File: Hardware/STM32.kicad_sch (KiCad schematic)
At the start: 70 parts, among them IC1 STTS22HTR, SW1 SW_Push_Dual, U3 STM32L4R5ZITx, Y2 TG-3541CE_32.7680KXB3, Y3 ECS-TXO-2520-33-250-AN-TR

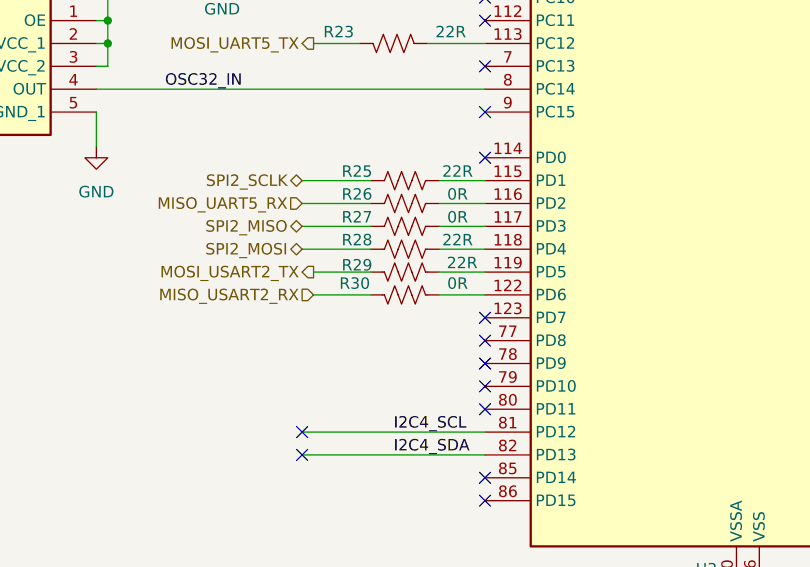
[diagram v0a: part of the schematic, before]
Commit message: Replace Optical Downlink with ADCS Sensors connector
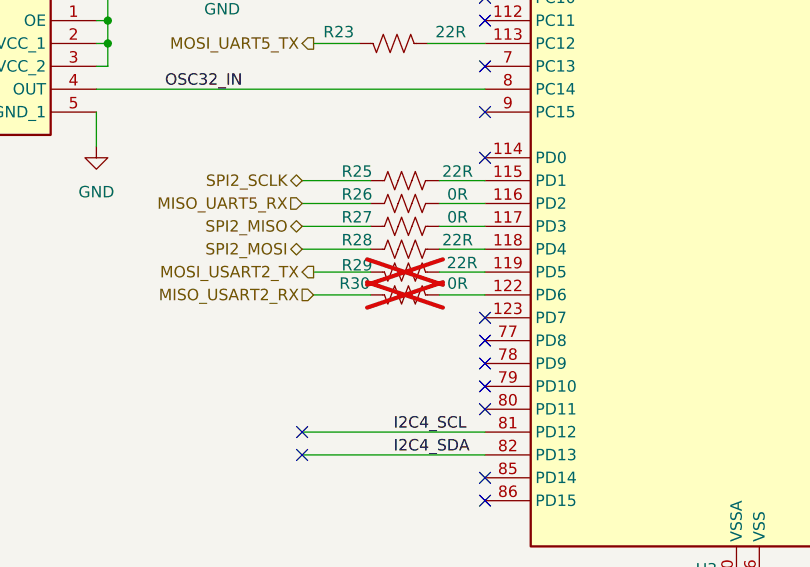
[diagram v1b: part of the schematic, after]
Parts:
- R29, R30: now not fitted
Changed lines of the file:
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@@
 		(in_bom yes)
 		(on_board yes)
-		(dnp no)
+		(dnp yes)
 		(property "Reference" "R29"
 			(at 172.466 215.138 90)
@@
 		(in_bom yes)
 		(on_board yes)
-		(dnp no)
+		(dnp yes)
 		(property "Reference" "R30"
 			(at 172.212 217.17 90)

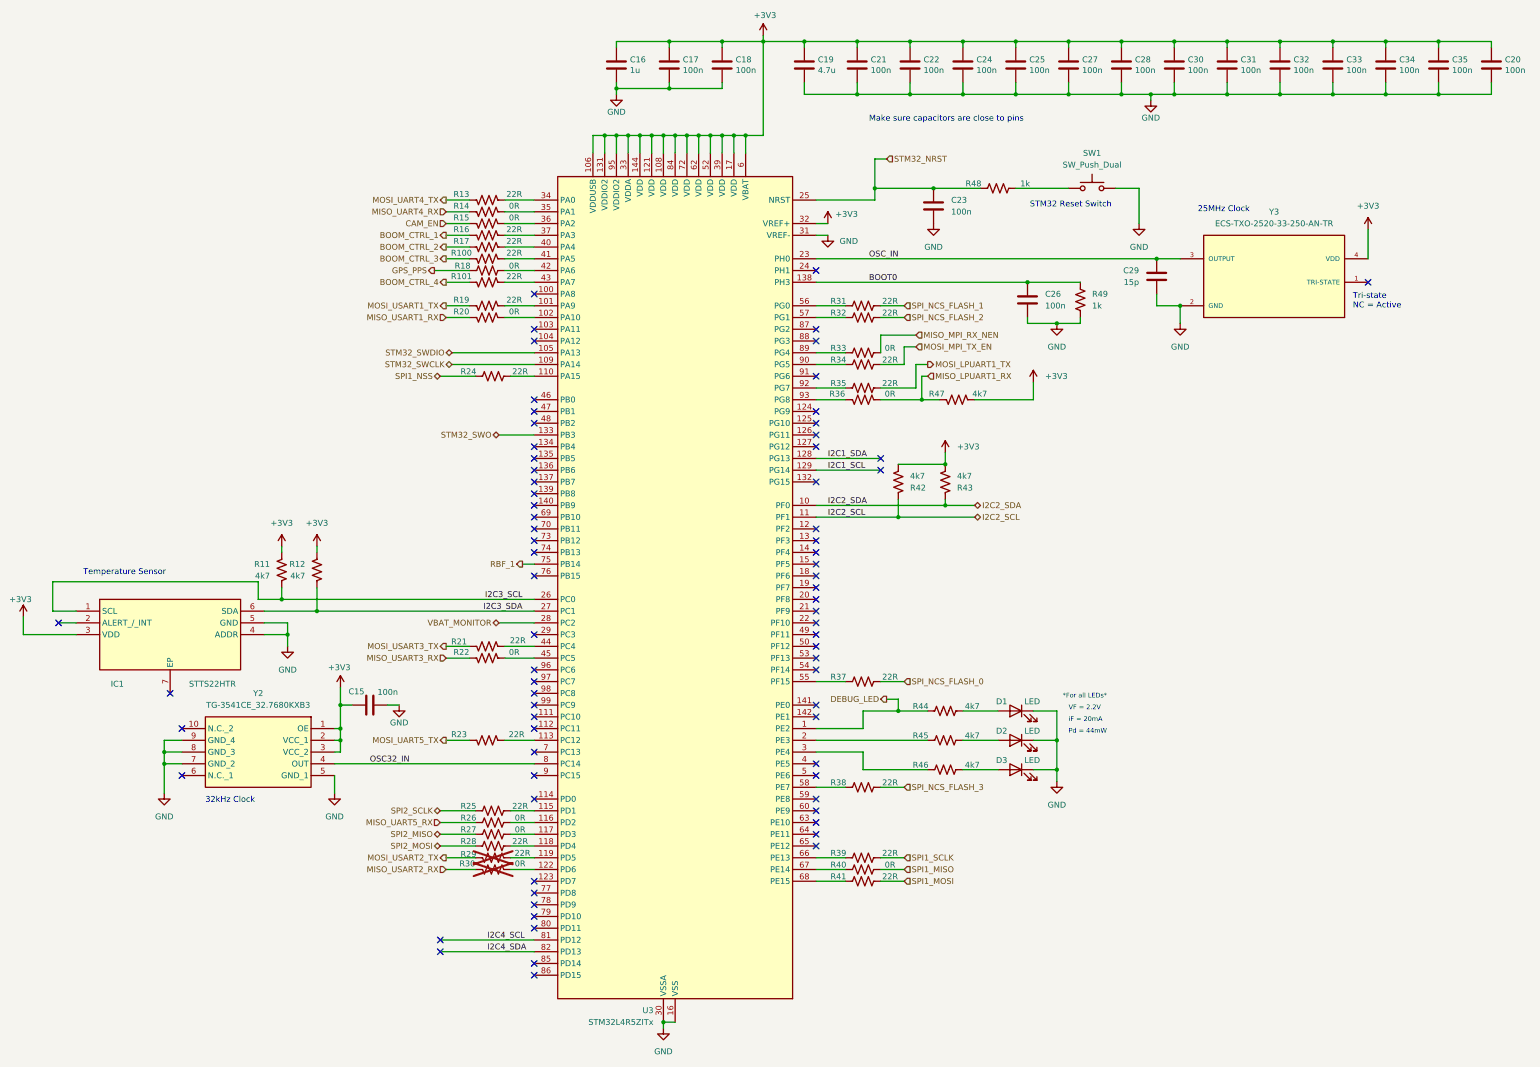
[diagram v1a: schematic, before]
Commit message: Update schematic to allow using STM32 alone
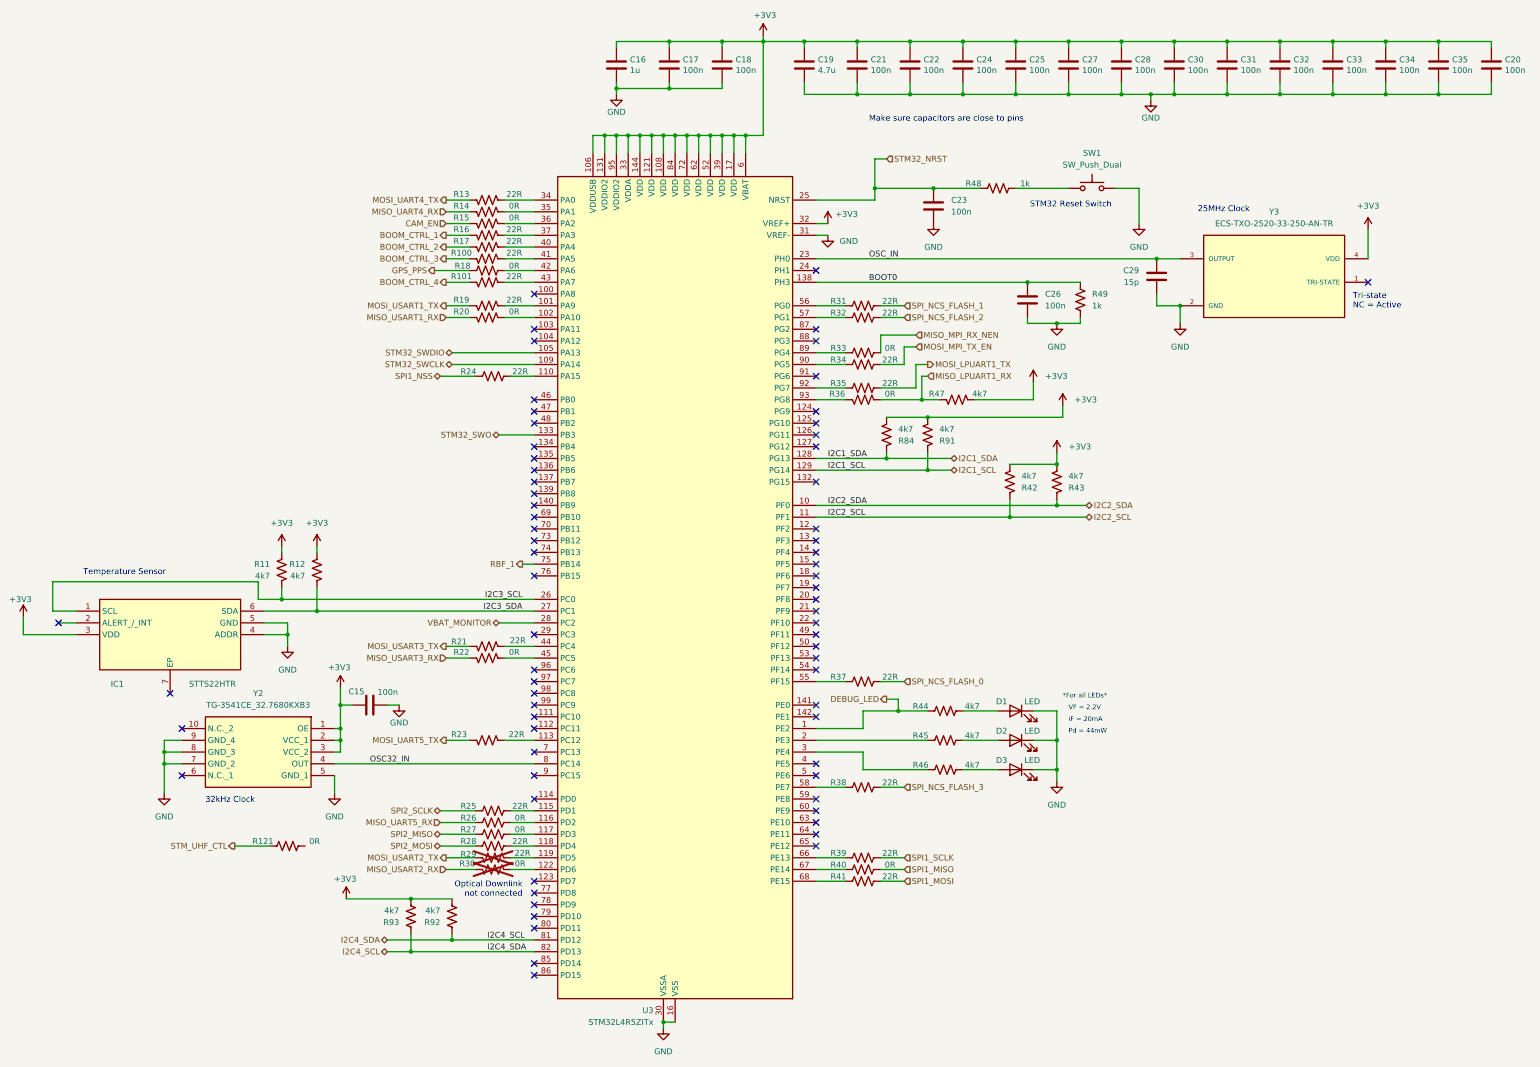
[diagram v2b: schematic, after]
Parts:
- added R121: 0R, Resistor_SMD:R_0603_1608Metric, symbol Device:R_US
- added R84, R91, R92, R93: 4k7, Resistor_SMD:R_0603_1608Metric, symbol Device:R_US
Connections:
- net I2C4_SDA is gone; now on net I2C4_SCL: U3.82 (PD13)
- net +3V3: now also R84.2, R91.2, R92.2, R93.2
- net I2C1_SCL: now also R91.1
- net I2C1_SDA: now also R84.1
- net I2C4_SCL: now also R92.1, R93.1
- new net STM_UHF_CTL: R121.1
- no-connect marks 74 -> 70
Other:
- note added: "Optical Downlink not connected"
- moved on the sheet: R42, R43

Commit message: Populate more resistors
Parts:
- removed R121: 0R, Resistor_SMD:R_0603_1608Metric, symbol Device:R_US
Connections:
- net I2C4_SCL: no longer R93.1, U3.82 (PD13)
- new net I2C4_SDA: R93.1, U3.82 (PD13)
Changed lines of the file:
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@@
 		)
 	)
-	(hierarchical_label "I2C4_SDA"
+	(hierarchical_label "I2C4_SCL"
 		(shape bidirectional)
 		(at 154.94 233.68 180)
@@
 		)
 	)
-	(hierarchical_label "I2C4_SCL"
+	(hierarchical_label "I2C4_SDA"
 		(shape bidirectional)
 		(at 154.94 236.22 180)
@@
 					(unit 1)
 				)
-			)
-		)
-	)
-	(symbol
-		(lib_id "Device:R_US")
-		(at 133.35 213.36 90)
-		(unit 1)
-		(exclude_from_sim no)
-		(in_bom yes)
-		(on_board yes)
-		(dnp no)
-		(property "Reference" "R121"
-			(at 128.016 212.344 90)
-			(effects
-				(font
-					(size 1.27 1.27)
-				)
-			)
-		)
-		(property "Value" "0R"
-			(at 139.192 212.344 90)
-			(effects
-				(font
-					(size 1.27 1.27)
-				)
-			)
-		)
-		(property "Footprint" "Resistor_SMD:R_0603_1608Metric"
-			(at 133.604 212.344 90)
-			(effects
-				(font
-					(size 1.27 1.27)
-				)
-				(hide yes)
-			)
-		)
-		(property "Datasheet" "~"
-			(at 133.35 213.36 0)
-			(effects
-				(font
-					(size 1.27 1.27)
-				)
-				(hide yes)
-			)
-		)
-		(property "Description" "Resistor, US symbol"
-			(at 133.35 213.36 0)
-			(effects
-				(font
-					(size 1.27 1.27)
-				)
-				(hide yes)
-			)
-		)
-		(pin "2"
-		)
-		(pin "1"
-		)
-		(instances
-			(project "CTS-SAT-2-OBC-PCB"
-				(path "/58243925-df8d-4fc1-899e-fce866d1d25a/c7b2a9f5-c39c-4892-aa33-31b3626fafef"
-					(reference "R121")
-					(unit 1)
-				)

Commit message: route most connectors
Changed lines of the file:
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@@
 	(wire
 		(pts
+			(xy 334.01 151.13) (xy 331.47 151.13)
+		)
+		(stroke
+			(width 0)
+			(type default)
+		)
+	)
+	(wire
+		(pts
 			(xy 290.83 50.8) (xy 279.4 50.8)
 		)
@@
 	(wire
 		(pts
+			(xy 334.01 148.59) (xy 331.47 148.59)
+		)
+		(stroke
+			(width 0)
+			(type default)
+		)
+	)
+	(wire
+		(pts
 			(xy 302.26 39.37) (xy 313.69 39.37)
 		)
@@
 	(wire
 		(pts
+			(xy 334.01 166.37) (xy 331.47 166.37)
+		)
+		(stroke
+			(width 0)
+			(type default)
+		)
+	)
+	(wire
+		(pts
 			(xy 232.41 59.69) (xy 232.41 63.5)
 		)
@@
 	(wire
 		(pts
+			(xy 334.01 161.29) (xy 331.47 161.29)
+		)
+		(stroke
+			(width 0)
+			(type default)
+		)
+	)
+	(wire
+		(pts
 			(xy 261.62 106.68) (xy 261.62 102.87)
 		)
@@
 	(wire
 		(pts
+			(xy 334.01 163.83) (xy 331.47 163.83)
+		)
+		(stroke
+			(width 0)
+			(type default)
+		)
+	)
+	(wire
+		(pts
 			(xy 180.34 88.9) (xy 186.69 88.9)
 		)
@@
 	(wire
 		(pts
+			(xy 334.01 158.75) (xy 331.47 158.75)
+		)
+		(stroke
+			(width 0)
+			(type default)
+		)
+	)
+	(wire
+		(pts
 			(xy 215.9 49.53) (xy 215.9 48.26)
 		)
@@
 	(wire
 		(pts
+			(xy 334.01 153.67) (xy 331.47 153.67)
+		)
+		(stroke
+			(width 0)
+			(type default)
+		)
+	)
+	(wire
+		(pts
 			(xy 201.93 59.69) (xy 201.93 63.5)
 		)
@@
 	(wire
 		(pts
+			(xy 334.01 156.21) (xy 331.47 156.21)
+		)
+		(stroke
+			(width 0)
+			(type default)
+		)
+	)
+	(wire
+		(pts
 			(xy 289.56 138.43) (xy 289.56 142.24)
 		)
@@
 		)
 	)
+	(wire
+		(pts
+			(xy 334.01 168.91) (xy 331.47 168.91)
+		)
+		(stroke
+			(width 0)
+			(type default)
+		)
+	)
 	(label "I2C3_SCL"
 		(at 184.15 160.02 180)
@@
 		)
 	)
+	(hierarchical_label "ADCS_CSS_2"
+		(shape input)
+		(at 334.01 158.75 0)
+		(effects
+			(font
+				(size 1.27 1.27)
+			)
+			(justify left)
+		)
+	)
 	(hierarchical_label "SPI_NCS_FLASH_2"
 		(shape input)
@@
 		)
 	)
+	(hierarchical_label "ADCS_CSS_3"
+		(shape input)
+		(at 334.01 161.29 0)
+		(effects
+			(font
+				(size 1.27 1.27)
+			)
+			(justify left)
+		)
+	)
 	(hierarchical_label "MISO_LPUART1_RX"
 		(shape input)
@@
 		)
 	)
+	(hierarchical_label "ADCS_MTM_IN"
+		(shape input)
+		(at 334.01 148.59 0)
+		(effects
+			(font
+				(size 1.27 1.27)
+			)
+			(justify left)
+		)
+	)
 	(hierarchical_label "MISO_MPI_RX_NEN"
 		(shape input)
@@
 		)
 	)
+	(hierarchical_label "ADCS_CSS_5"
+		(shape input)
+		(at 334.01 166.37 0)
+		(effects
+			(font
+				(size 1.27 1.27)
+			)
+			(justify left)
+		)
+	)
 	(hierarchical_label "STM_UHF_CTL"
 		(shape output)
@@
 		)
 	)
+	(hierarchical_label "ADCS_CSS_6"
+		(shape input)
+		(at 334.01 168.91 0)
+		(effects
+			(font
+				(size 1.27 1.27)
+			)
+			(justify left)
+		)
+	)
 	(hierarchical_label "VBAT_MONITOR"
 		(shape bidirectional)
@@
 		)
 	)
+	(hierarchical_label "ADCS_FSS_2"
+		(shape input)
+		(at 334.01 153.67 0)
+		(effects
+			(font
+				(size 1.27 1.27)
+			)
+			(justify left)
+		)
+	)
 	(hierarchical_label "STM32_SWO"
 		(shape bidirectional)
@@
 		)
 	)
+	(hierarchical_label "ADCS_FSS_1"
+		(shape input)
+		(at 334.01 151.13 0)
+		(effects
+			(font
+				(size 1.27 1.27)
+			)
+			(justify left)
+		)
+	)
 	(hierarchical_label "SPI2_MOSI"
 		(shape bidirectional)
@@
 		)
 	)
+	(hierarchical_label "ADCS_CSS_4"
+		(shape input)
+		(at 334.01 163.83 0)
+		(effects
+			(font
+				(size 1.27 1.27)
+			)
+			(justify left)
+		)
+	)
 	(hierarchical_label "STM32_SWCLK"
 		(shape bidirectional)
@@
 		)
 	)
+	(hierarchical_label "ADCS_CSS_1"
+		(shape input)
+		(at 334.01 156.21 0)
+		(effects
+			(font
+				(size 1.27 1.27)
+			)
+			(justify left)
+		)
+	)
